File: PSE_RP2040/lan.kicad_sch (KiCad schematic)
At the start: 32 parts, among them IC1 LAN8742A-CZ, T1 749013011, U4 USBLC6-4SC6

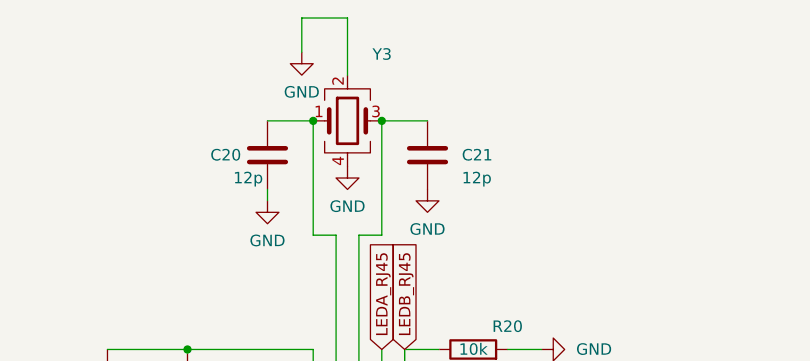
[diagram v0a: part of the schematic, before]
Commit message: footprint
cambiato footprint rp2040 (ora c'è quello con le vias) e footprint tps2375
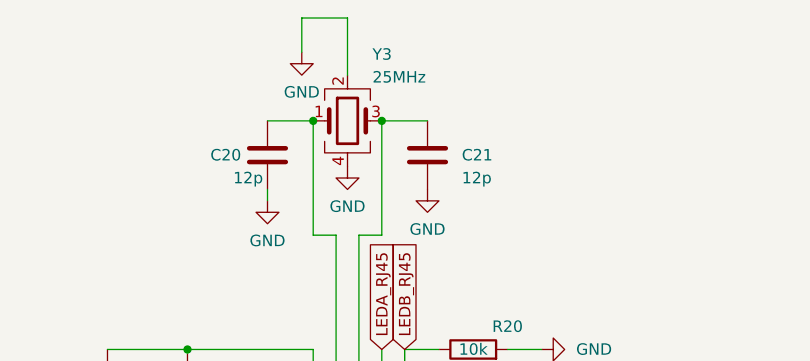
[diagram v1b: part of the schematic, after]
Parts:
- Y3: value (none) -> 25MHz; footprint (none) -> Crystal:Crystal_SMD_3225-4Pin_3.2x2.5mm_HandSoldering
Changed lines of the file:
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@@
       (effects (font (size 1.27 1.27)) (justify left))
     )
-    (property "Value" "" (id 1) (at 98.0187 25.6341 0)
+    (property "Value" "25MHz" (id 1) (at 98.0187 25.6341 0)
       (effects (font (size 1.27 1.27)) (justify left))
     )
-    (property "Footprint" "" (id 2) (at 95.25 30.48 0)
+    (property "Footprint" "Crystal:Crystal_SMD_3225-4Pin_3.2x2.5mm_HandSoldering" (id 2) (at 95.25 30.48 0)
       (effects (font (size 1.27 1.27)) hide)
     )

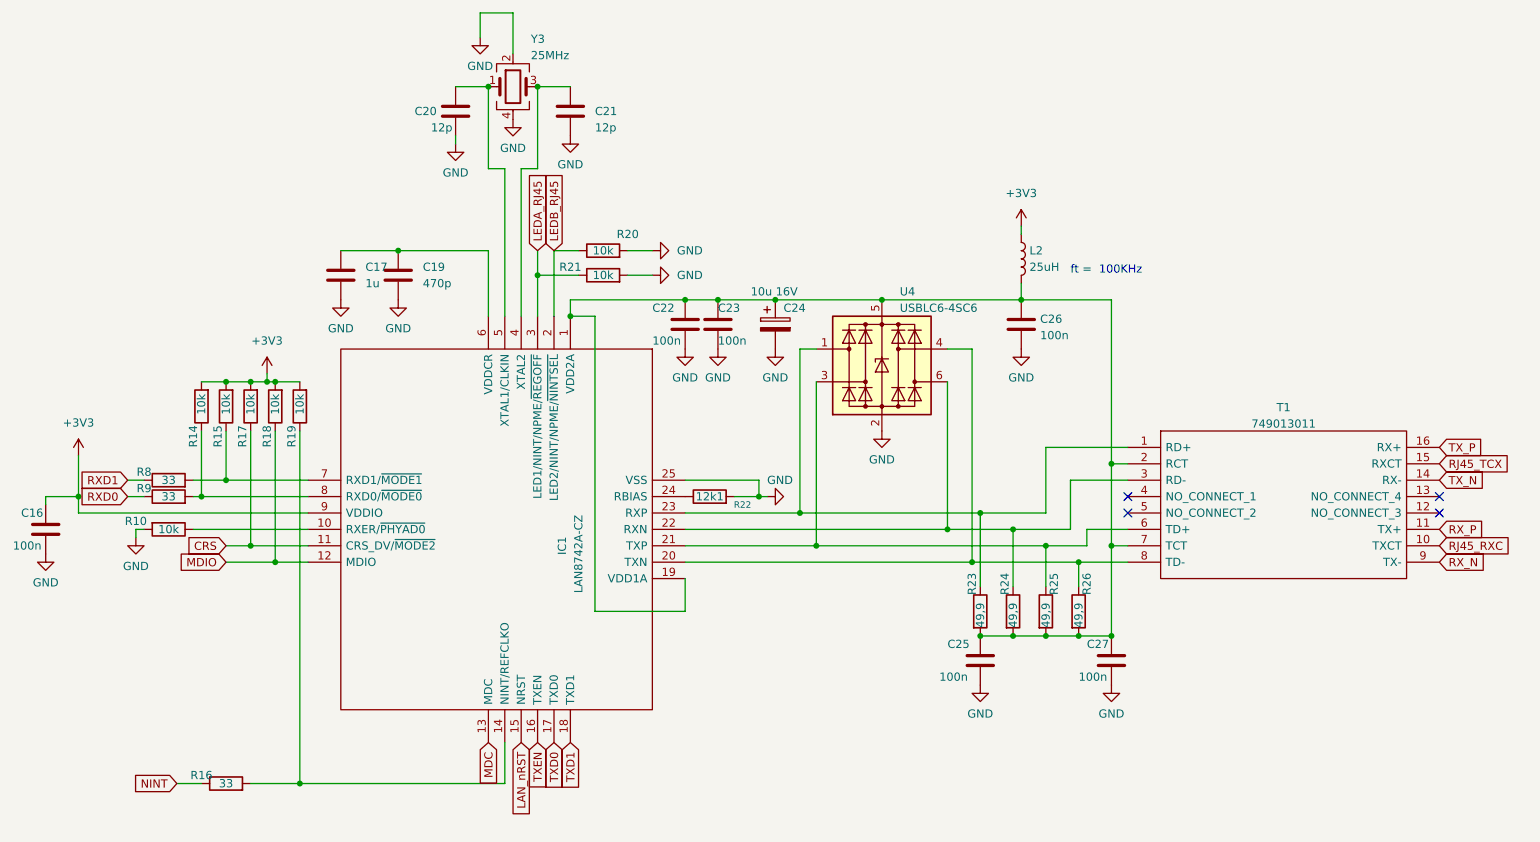
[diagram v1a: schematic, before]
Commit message: check pin, footprint e symb mem
tolto pin 9 al simbolo memoria
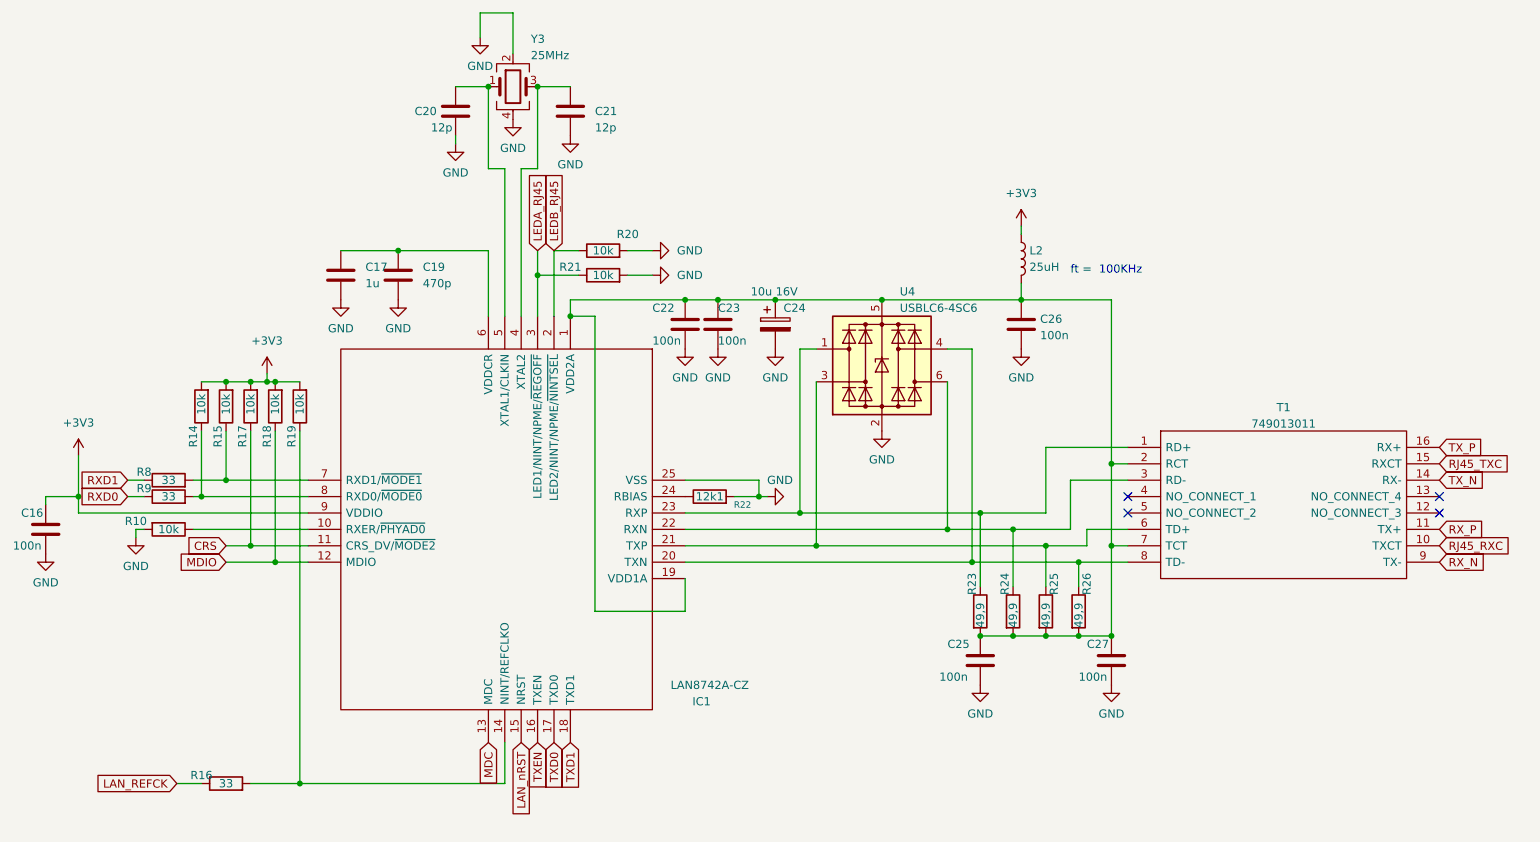
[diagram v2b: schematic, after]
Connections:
- net NINT renamed LAN_REFCK
- net RJ45_TCX renamed RJ45_TXC
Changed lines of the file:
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@@
     )
   )
-  (global_label "RJ45_TCX" (shape input) (at 238.76 88.9 0) (fields_autoplaced)
+  (global_label "RJ45_TXC" (shape input) (at 238.76 88.9 0) (fields_autoplaced)
     (effects (font (size 1.27 1.27)) (justify left))
     (property "Intersheet References" "${INTERSHEET_REFS}" (id 0) (at 250.1556 88.8206 0)
@@
     )
   )
-  (global_label "NINT" (shape input) (at 43.18 138.43 180) (fields_autoplaced)
-    (effects (font (size 1.27 1.27)) (justify right))
-    (property "Intersheet References" "${INTERSHEET_REFS}" (id 0) (at 36.6225 138.3506 0)
+  (global_label "LAN_REFCK" (shape input) (at 43.18 138.43 180) (fields_autoplaced)
+    (effects (font (size 1.27 1.27)) (justify right))
+    (property "Intersheet References" "${INTERSHEET_REFS}" (id 0) (at 30.3934 138.3506 0)
       (effects (font (size 1.27 1.27)) (justify right) hide)
     )
@@
   (symbol (lib_id "ethernet:LAN8742A-CZ") (at 104.14 66.04 270) (unit 1)
     (in_bom yes) (on_board yes)
-    (property "Reference" "IC1" (id 0) (at 102.87 101.6 0))
-    (property "Value" "LAN8742A-CZ" (id 1) (at 105.41 102.87 0))
+    (property "Reference" "IC1" (id 0) (at 124.46 125.73 90))
+    (property "Value" "LAN8742A-CZ" (id 1) (at 125.73 123.19 90))
     (property "Footprint" "Package_DFN_QFN:HVQFN-24-1EP_4x4mm_P0.5mm_EP2.5x2.5mm_ThermalVias" (id 2) (at 116.84 128.27 0)
       (effects (font (size 1.27 1.27)) (justify left) hide)

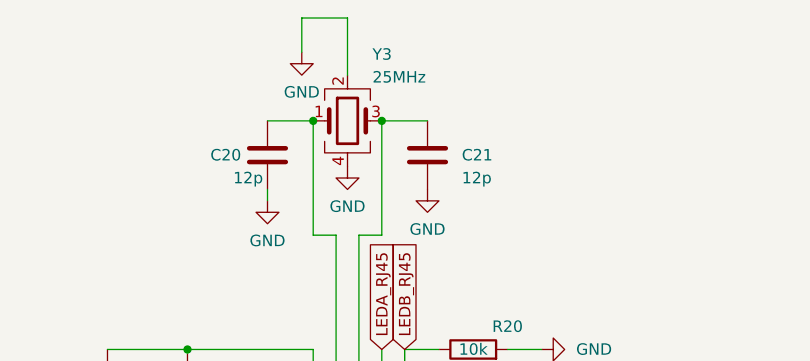
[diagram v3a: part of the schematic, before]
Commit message: pad micro, footprint, posizionamento componenti pcb
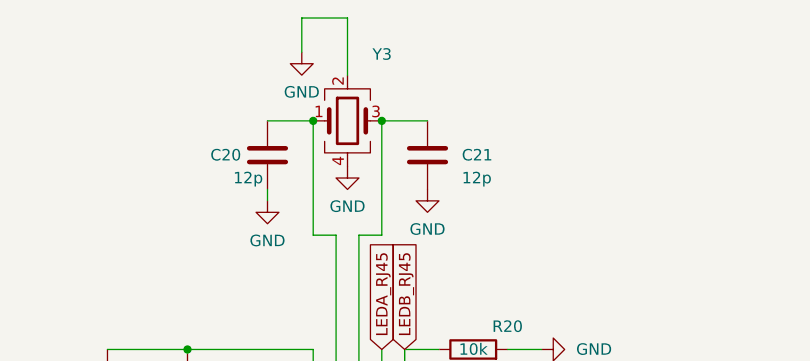
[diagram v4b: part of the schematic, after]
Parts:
- Y3: value 25MHz -> (none); footprint Crystal:Crystal_SMD_3225-4Pin_3.2x2.5mm_HandSoldering -> (none)
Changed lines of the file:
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@@
       (effects (font (size 1.27 1.27)) (justify left))
     )
-    (property "Value" "25MHz" (id 1) (at 98.0187 25.6341 0)
+    (property "Value" "" (id 1) (at 98.0187 25.6341 0)
       (effects (font (size 1.27 1.27)) (justify left))
     )
-    (property "Footprint" "Crystal:Crystal_SMD_3225-4Pin_3.2x2.5mm_HandSoldering" (id 2) (at 95.25 30.48 0)
+    (property "Footprint" "" (id 2) (at 95.25 30.48 0)
       (effects (font (size 1.27 1.27)) hide)
     )

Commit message: piazzamento componenti pcb
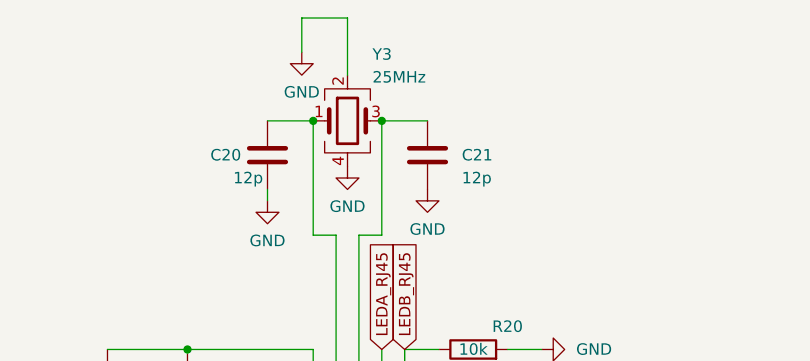
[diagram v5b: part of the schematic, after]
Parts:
- Y3: value (none) -> 25MHz; footprint (none) -> Crystal:Crystal_SMD_3225-4Pin_3.2x2.5mm
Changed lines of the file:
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@@
       (effects (font (size 1.27 1.27)) (justify left))
     )
-    (property "Value" "" (id 1) (at 98.0187 25.6341 0)
+    (property "Value" "25MHz" (id 1) (at 98.0187 25.6341 0)
       (effects (font (size 1.27 1.27)) (justify left))
     )
-    (property "Footprint" "" (id 2) (at 95.25 30.48 0)
+    (property "Footprint" "Crystal:Crystal_SMD_3225-4Pin_3.2x2.5mm" (id 2) (at 95.25 30.48 0)
       (effects (font (size 1.27 1.27)) hide)
     )

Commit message: pcb merdaccia
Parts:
- C16, C22, C23, C25, C26, C27: value 100n -> (none); footprint Capacitor_SMD:C_0603_1608Metric -> (none)
- C17: value 1u -> (none); footprint Capacitor_SMD:C_0603_1608Metric -> (none)
- C19: value 470p -> (none); footprint Capacitor_SMD:C_0603_1608Metric -> (none)
- C20, C21: value 12p -> (none); footprint Capacitor_SMD:C_0603_1608Metric -> (none)
- C24: value 10u 16V -> (none); footprint Capacitor_SMD:C_0805_2012Metric -> (none)
- IC1: value LAN8742A-CZ -> (none); footprint Package_DFN_QFN:HVQFN-24-1EP_4x4mm_P0.5mm_EP2.5x2.5mm_ThermalVias -> (none)
- L2: value 25uH -> (none); footprint Inductor_SMD:L_0603_1608Metric -> (none)
- R10, R14, R15, R17, R18, R19, R20, R21: value 10k -> (none); footprint Resistor_SMD:R_0603_1608Metric -> (none)
- R16, R8, R9: value 33 -> (none); footprint Resistor_SMD:R_0603_1608Metric -> (none)
- R22: value 12k1 -> (none); footprint Resistor_SMD:R_0603_1608Metric -> (none)
- R23, R24, R25, R26: value 49,9 -> (none); footprint Resistor_SMD:R_0603_1608Metric -> (none)
- T1: value 749013011 -> (none); footprint Transformer_SMD:Transformer_Ethernet_Wuerth_749013011A -> (none)
- U4: value USBLC6-4SC6 -> (none); footprint Package_TO_SOT_SMD:SOT-23-6 -> (none)
- Y3: value 25MHz -> (none); footprint Crystal:Crystal_SMD_3225-4Pin_3.2x2.5mm -> (none)

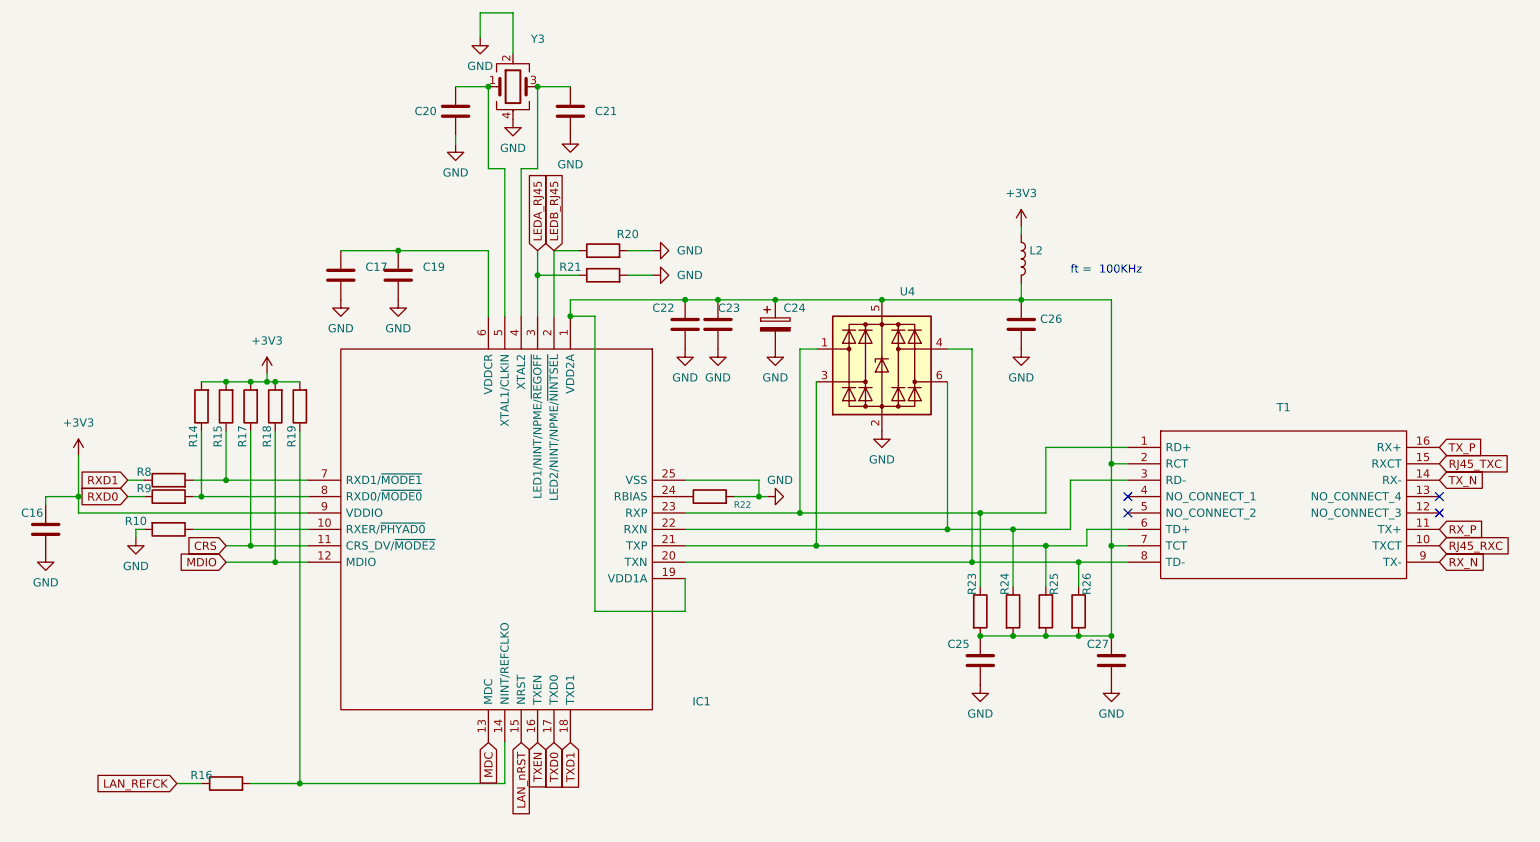
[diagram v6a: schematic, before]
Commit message: PCB
Aggiunto strato rame bottom, tolto mounting hole 4 dallo schematico, aggiunti fiducial (solo sul PCB), riduzione margine scheda, sbroglio.
(larghezza max piste in uscita dal micro 7 mils)
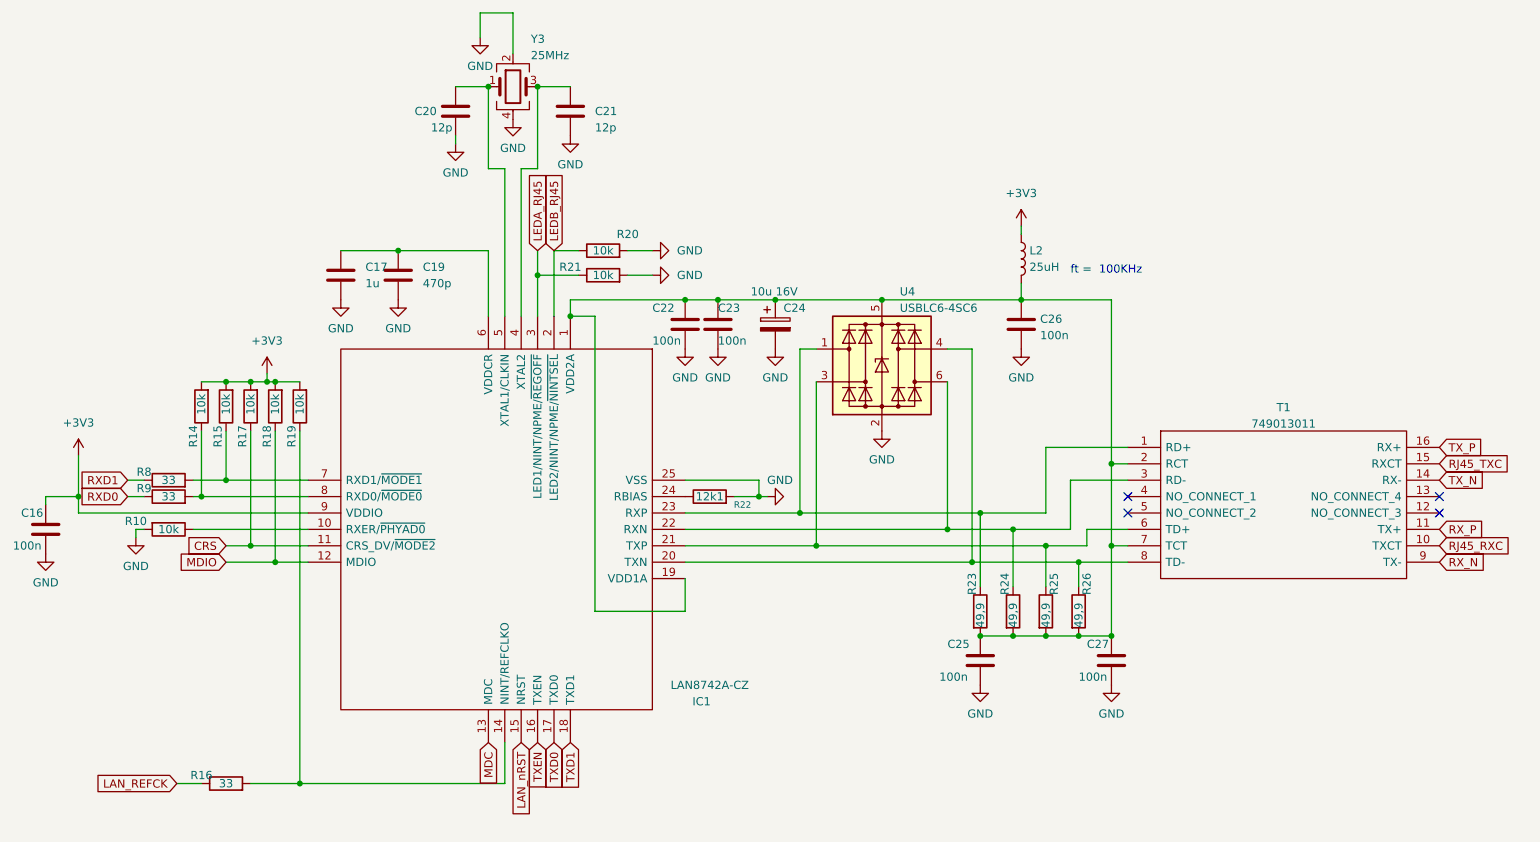
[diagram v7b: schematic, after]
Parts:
- C16, C22, C23, C25, C26, C27: value (none) -> 100n; footprint (none) -> Capacitor_SMD:C_0603_1608Metric
- C17: value (none) -> 1u; footprint (none) -> Capacitor_SMD:C_0603_1608Metric
- C19: value (none) -> 470p; footprint (none) -> Capacitor_SMD:C_0603_1608Metric
- C20, C21: value (none) -> 12p; footprint (none) -> Capacitor_SMD:C_0603_1608Metric
- C24: value (none) -> 10u 16V; footprint (none) -> Capacitor_SMD:C_0805_2012Metric
- IC1: value (none) -> LAN8742A-CZ; footprint (none) -> Package_DFN_QFN:HVQFN-24-1EP_4x4mm_P0.5mm_EP2.5x2.5mm_ThermalVias
- L2: value (none) -> 25uH; footprint (none) -> Inductor_SMD:L_0603_1608Metric
- R10, R14, R15, R17, R18, R19, R20, R21: value (none) -> 10k; footprint (none) -> Resistor_SMD:R_0603_1608Metric
- R16, R8, R9: value (none) -> 33; footprint (none) -> Resistor_SMD:R_0603_1608Metric
- R22: value (none) -> 12k1; footprint (none) -> Resistor_SMD:R_0603_1608Metric
- R23, R24, R25, R26: value (none) -> 49,9; footprint (none) -> Resistor_SMD:R_0603_1608Metric
- T1: value (none) -> 749013011; footprint (none) -> Transformer_SMD:Transformer_Ethernet_Wuerth_749013011A
- U4: value (none) -> USBLC6-4SC6; footprint (none) -> Package_TO_SOT_SMD:SOT-23-6
- Y3: value (none) -> 25MHz; footprint (none) -> Crystal:Crystal_SMD_3225-4Pin_3.2x2.5mm
